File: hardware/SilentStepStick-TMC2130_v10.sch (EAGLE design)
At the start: 26 parts, among them IC1 TMC2130-LA, X1 PASSER-07, X2 PASSER-07

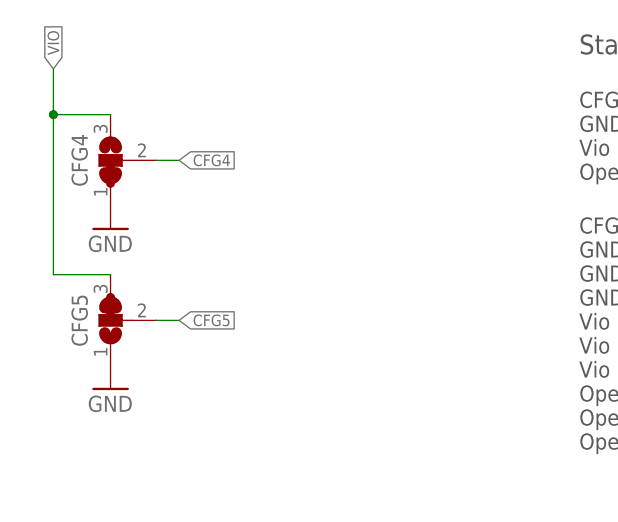
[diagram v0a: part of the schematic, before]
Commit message: updated schematics
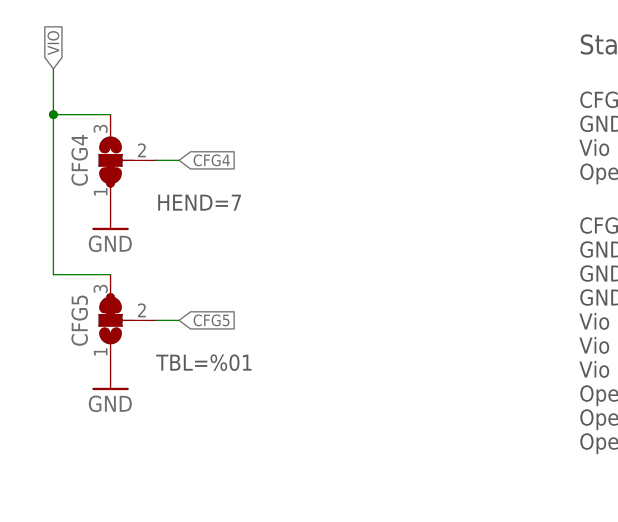
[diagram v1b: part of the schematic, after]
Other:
- note added: "HEND=7"
- note added: "TBL=%01"
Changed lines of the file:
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@@
 <?xml version="1.0" encoding="utf-8"?>
 <!DOCTYPE eagle SYSTEM "eagle.dtd">
-<eagle version="7.6.0">
+<eagle version="7.7.0">
 <drawing>
 <settings>
@@
 <setting verticaltext="up"/>
 </settings>
-<grid distance="0.1" unitdist="inch" unit="inch" style="lines" multiple="1" display="no" altdistance="0.01" altunitdist="inch" altunit="inch"/>
+<grid distance="0.05" unitdist="inch" unit="inch" style="lines" multiple="1" display="yes" altdistance="0.025" altunitdist="inch" altunit="inch"/>
 <layers>
 <layer number="1" name="Top" color="4" fill="1" visible="no" active="no"/>
@@
 stealthChop</text>
 <text x="90.17" y="57.15" size="2.1844" layer="97" font="vector" ratio="10" align="top-left">Standalone Operation (SPI_MODE=GND)</text>
+<text x="43.18" y="39.37" size="1.778" layer="97" font="vector" ratio="10" align="top-left">HEND=7</text>
+<text x="43.18" y="21.59" size="1.778" layer="97" font="vector" ratio="10" align="top-left">TBL=%01</text>
 </plain>
 <instances>

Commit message: updated schematics
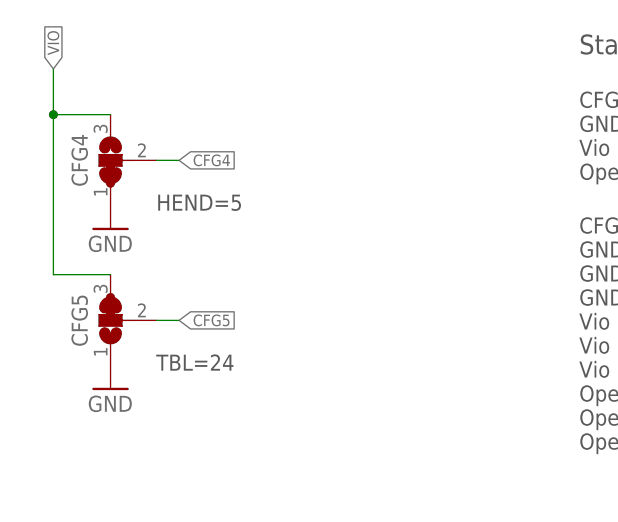
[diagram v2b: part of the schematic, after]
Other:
- note added: "HEND=5"
- note added: "TBL=24"
- note removed: "HEND=7"
- note removed: "TBL=%01"
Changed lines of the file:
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@@
 <setting verticaltext="up"/>
 </settings>
-<grid distance="0.05" unitdist="inch" unit="inch" style="lines" multiple="1" display="yes" altdistance="0.025" altunitdist="inch" altunit="inch"/>
+<grid distance="0.1" unitdist="inch" unit="inch" style="lines" multiple="1" display="no" altdistance="0.01" altunitdist="inch" altunit="inch"/>
 <layers>
 <layer number="1" name="Top" color="4" fill="1" visible="no" active="no"/>
@@
 stealthChop</text>
 <text x="90.17" y="57.15" size="2.1844" layer="97" font="vector" ratio="10" align="top-left">Standalone Operation (SPI_MODE=GND)</text>
-<text x="43.18" y="39.37" size="1.778" layer="97" font="vector" ratio="10" align="top-left">HEND=7</text>
-<text x="43.18" y="21.59" size="1.778" layer="97" font="vector" ratio="10" align="top-left">TBL=%01</text>
+<text x="43.18" y="39.37" size="1.778" layer="97" font="vector" ratio="10" align="top-left">HEND=5</text>
+<text x="43.18" y="21.59" size="1.778" layer="97" font="vector" ratio="10" align="top-left">TBL=24</text>
 </plain>
 <instances>
